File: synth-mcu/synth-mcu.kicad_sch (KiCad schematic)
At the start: 5 parts, among them J1 LoopMatrix, J2 AudioControls, J3 Conn_01x25_Socket, J4 Conn_01x25_Socket, J5 AUXOut

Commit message: add mounting holes to mcu pcb
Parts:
- added H1, H2, H3, H4: MountingHole, MountingHole:MountingHole_3.2mm_M3, symbol Mechanical:MountingHole
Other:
- note removed: "PC0 PC1 PC2 PC3 PA7 PC4 PC5 PB0 PB1"

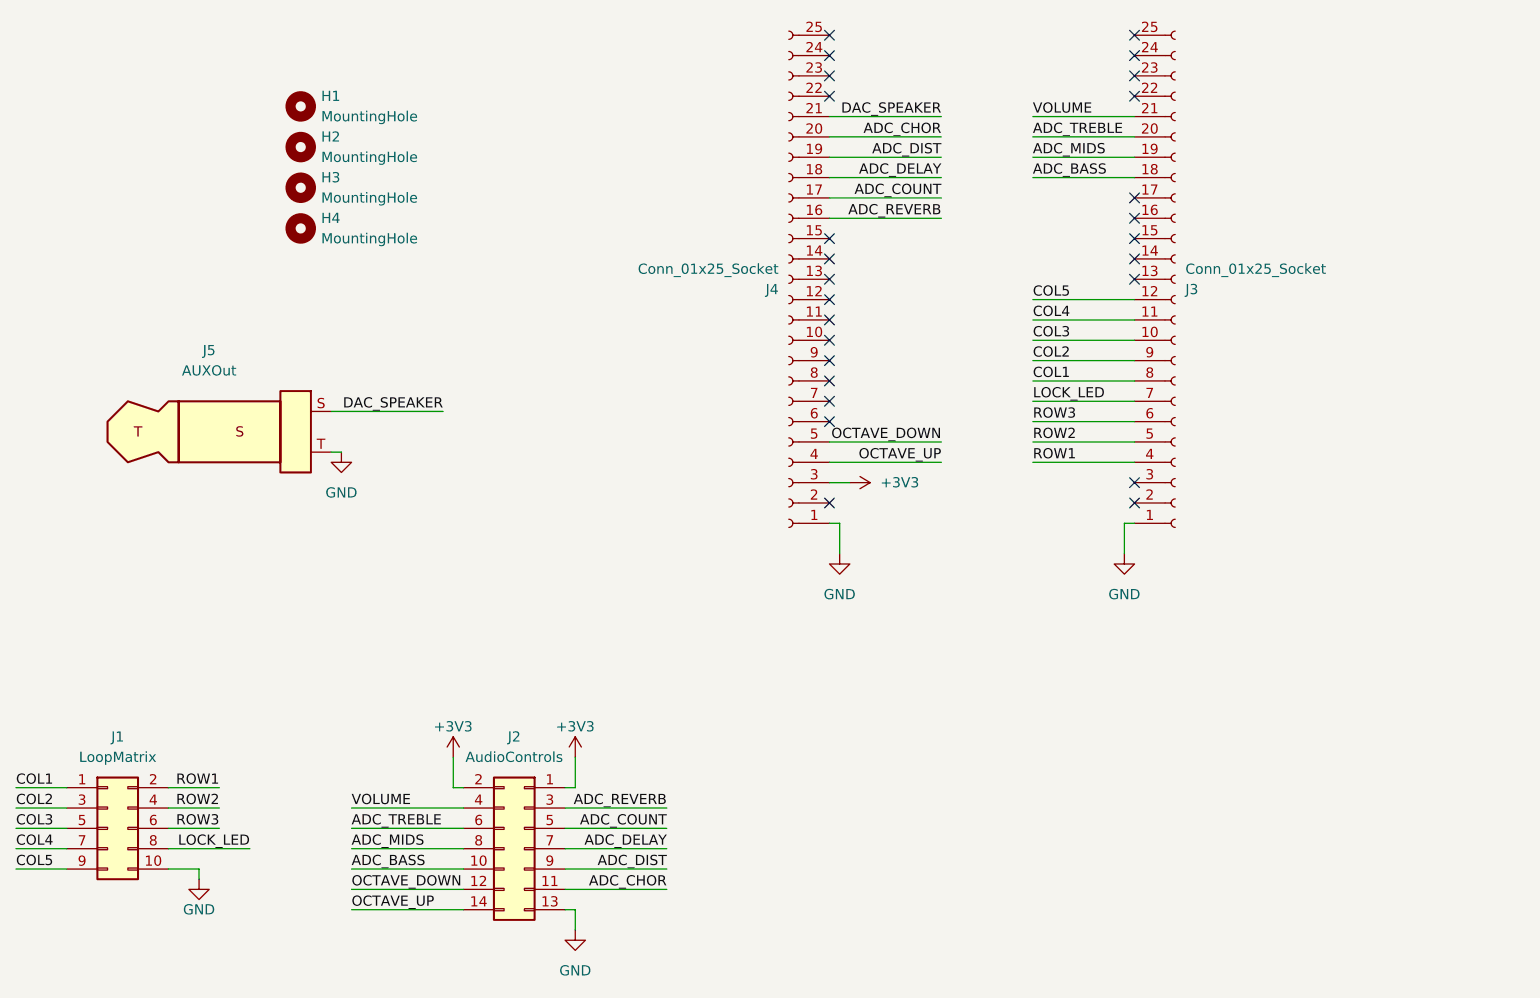
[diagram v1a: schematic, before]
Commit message: GPIO breakout for MCU board
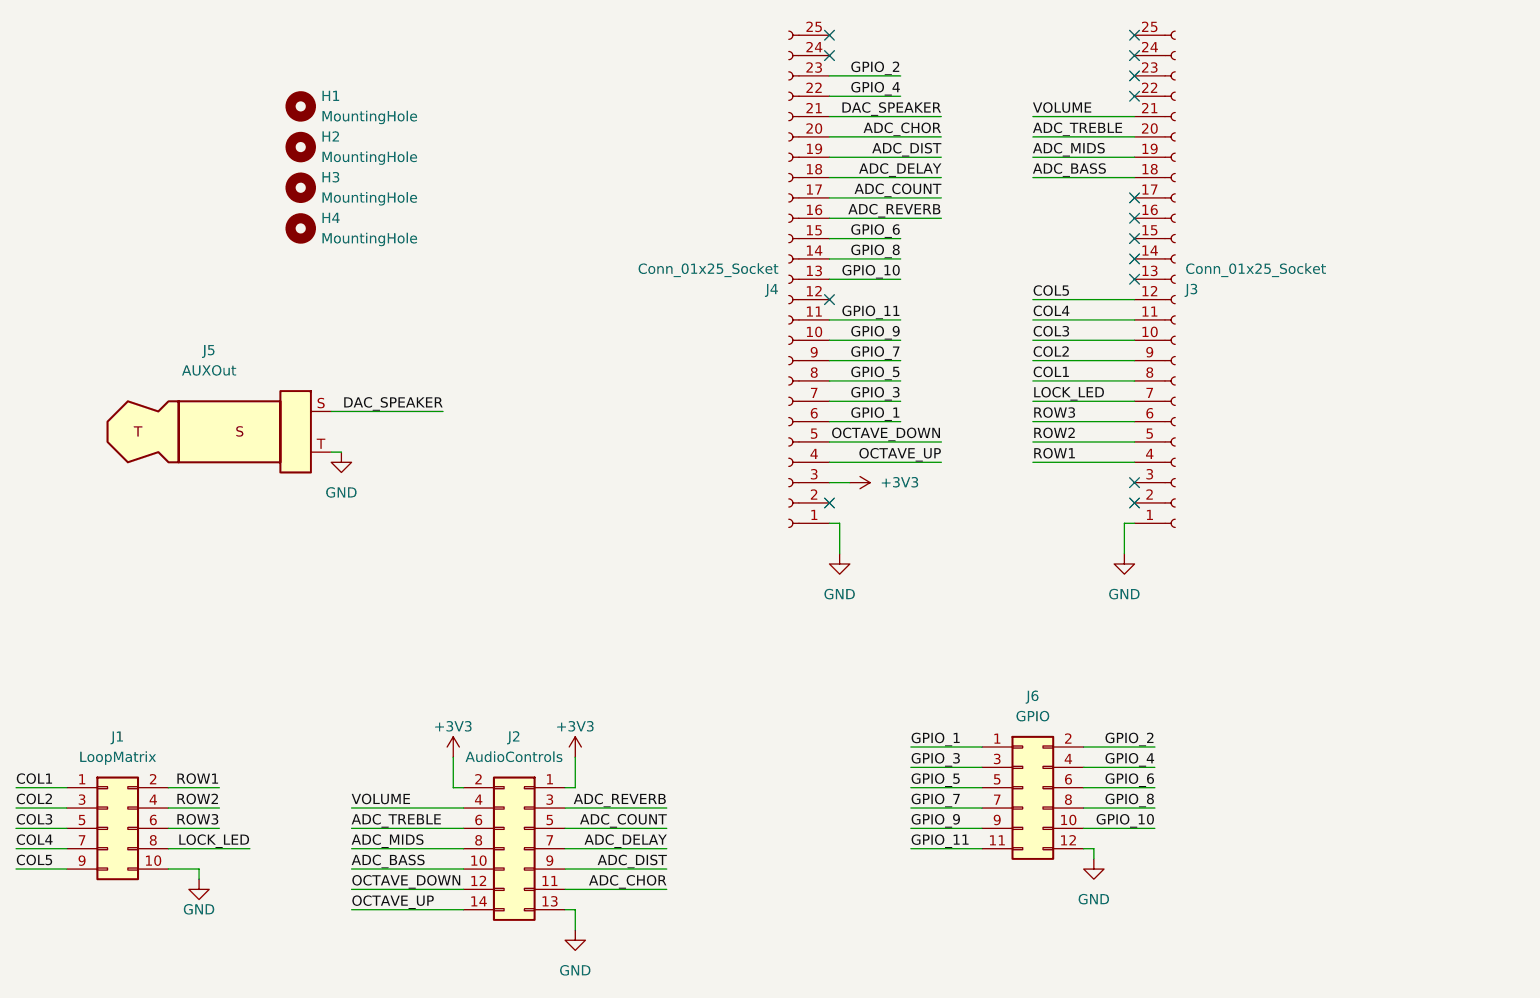
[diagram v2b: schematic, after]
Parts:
- added J6: GPIO, Connector_IDC:IDC-Header_2x06_P2.54mm_Vertical, symbol Connector_Generic:Conn_02x06_Odd_Even
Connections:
- net GND: now also J6.12 (Pin_12)
- net GPIO_9: now reaches J4.10 (Pin_10)
- net GPIO_9: now also J6.9 (Pin_9)
- net GPIO_11: now reaches J4.11 (Pin_11)
- net GPIO_11: now also J6.11 (Pin_11)
- net GPIO_10: now reaches J4.13 (Pin_13)
- net GPIO_10: now also J6.10 (Pin_10)
- net GPIO_8: now reaches J4.14 (Pin_14)
- net GPIO_8: now also J6.8 (Pin_8)
- net GPIO_6: now reaches J4.15 (Pin_15)
- net GPIO_6: now also J6.6 (Pin_6)
- net GPIO_4: now reaches J4.22 (Pin_22)
- net GPIO_4: now also J6.4 (Pin_4)
- net GPIO_2: now reaches J4.23 (Pin_23)
- net GPIO_2: now also J6.2 (Pin_2)
- net GPIO_1: now reaches J4.6 (Pin_6)
- net GPIO_1: now also J6.1 (Pin_1)
- net GPIO_3: now reaches J4.7 (Pin_7)
- net GPIO_3: now also J6.3 (Pin_3)
- net GPIO_5: now reaches J4.8 (Pin_8)
- net GPIO_5: now also J6.5 (Pin_5)
- net GPIO_7: now reaches J4.9 (Pin_9)
- net GPIO_7: now also J6.7 (Pin_7)
- no-connect marks 26 -> 15

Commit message: implement design suggestions from TA
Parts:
- removed J6: GPIO, Connector_IDC:IDC-Header_2x06_P2.54mm_Vertical, symbol Connector_Generic:Conn_02x06_Odd_Even
- added J7: GPIO, Connector_IDC:IDC-Header_2x07_P2.54mm_Vertical, symbol Connector_Generic:Conn_02x07_Odd_Even
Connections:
- net GND: now also J7.14 (Pin_14)
- net GPIO_1: now also J7.1 (Pin_1)
- net GPIO_10: now also J7.10 (Pin_10)
- net GPIO_11: now also J7.11 (Pin_11)
- net GPIO_2: now also J7.2 (Pin_2)
- net GPIO_3: now also J7.3 (Pin_3)
- net GPIO_4: now also J7.4 (Pin_4)
- net GPIO_5: now also J7.5 (Pin_5)
- net GPIO_6: now also J7.6 (Pin_6)
- net GPIO_7: now also J7.7 (Pin_7)
- net GPIO_8: now also J7.8 (Pin_8)
- net GPIO_9: now also J7.9 (Pin_9)
- new net GPIO_12: J7.12 (Pin_12)
- new net GPIO_13: J7.13 (Pin_13)
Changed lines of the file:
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@@
+	(wire
+		(pts
+			(xy 162.56 137.16) (xy 171.45 137.16)
+		)
+		(stroke
+			(width 0)
+			(type default)
+		)
+	)
 	(wire
 		(pts
@@
 	(wire
 		(pts
-			(xy 185.42 135.89) (xy 185.42 134.62)
-		)
-		(stroke
-			(width 0)
-			(type default)
-		)
-	)
-	(wire
-		(pts
 			(xy 90.17 80.01) (xy 104.14 80.01)
 		)
@@
 	(wire
 		(pts
+			(xy 185.42 137.16) (xy 184.15 137.16)
+		)
+		(stroke
+			(width 0)
+			(type default)
+		)
+	)
+	(wire
+		(pts
 			(xy 177.8 50.8) (xy 190.5 50.8)
 		)
@@
 	(wire
 		(pts
+			(xy 185.42 138.43) (xy 185.42 137.16)
+		)
+		(stroke
+			(width 0)
+			(type default)
+		)
+	)
+	(wire
+		(pts
 			(xy 120.65 123.19) (xy 120.65 127)
 		)
@@
 	(wire
 		(pts
-			(xy 184.15 134.62) (xy 185.42 134.62)
+			(xy 184.15 134.62) (xy 193.04 134.62)
 		)
 		(stroke
@@
 		)
 	)
+	(label "GPIO_12"
+		(at 193.04 134.62 180)
+		(effects
+			(font
+				(size 1.27 1.27)
+			)
+			(justify right bottom)
+		)
+	)
 	(label "LOCK_LED"
 		(at 177.8 78.74 0)
@@
 			)
 			(justify right bottom)
+		)
+	)
+	(label "GPIO_13"
+		(at 162.56 137.16 0)
+		(effects
+			(font
+				(size 1.27 1.27)
+			)
+			(justify left bottom)
 		)
 	)
@@
 	)
 	(symbol
-		(lib_id "Connector_Generic:Conn_02x06_Odd_Even")
-		(at 176.53 127 0)
-		(unit 1)
-		(body_style 1)
-		(exclude_from_sim no)
-		(in_bom yes)
-		(on_board yes)
-		(in_pos_files yes)
-		(dnp no)
-		(fields_autoplaced yes)
-		(property "Reference" "J6"
-			(at 177.8 115.57 0)
-			(show_name no)
-			(do_not_autoplace no)
-			(effects
-				(font
-					(size 1.27 1.27)
-				)
-			)
-		)
-		(property "Value" "GPIO"
-			(at 177.8 118.11 0)
-			(show_name no)
-			(do_not_autoplace no)
-			(effects
-				(font
-					(size 1.27 1.27)
-				)
-			)
-		)
-		(property "Footprint" "Connector_IDC:IDC-Header_2x06_P2.54mm_Vertical"
-			(at 176.53 127 0)
-			(hide yes)
-			(show_name no)
-			(do_not_autoplace no)
-			(effects
-				(font
-					(size 1.27 1.27)
-				)
-			)
-		)
-		(property "Datasheet" ""
-			(at 176.53 127 0)
-			(hide yes)
-			(show_name no)
-			(do_not_autoplace no)
-			(effects
-				(font
-					(size 1.27 1.27)
-				)
-			)
-		)
-		(property "Description" "Generic connector, double row, 02x06, odd/even pin numbering scheme (row 1 odd numbers, row 2 even numbers), script generated (kicad-library-utils/schlib/autogen/connector/)"
-			(at 176.53 127 0)
-			(hide yes)
-			(show_name no)
-			(do_not_autoplace no)
-			(effects
-				(font
-					(size 1.27 1.27)
-				)
-			)
-		)
-		(pin "12"
-		)
-		(pin "11"
-		)
-		(pin "1"
-		)
-		(pin "8"
-		)
-		(pin "7"
-		)
-		(pin "10"
-		)
-		(pin "9"
-		)
-		(pin "3"
-		)
-		(pin "5"
-		)
-		(pin "2"
-		)
-		(pin "4"
-		)
-		(pin "6"
-		)
-		(instances
-			(project "synth-mcu"
-				(path "/c088e41c-dfaf-4c9b-ad71-cd5bad59edb3"
-					(reference "J6")
-					(unit 1)
-				)
-			)
-		)
-	)
-	(symbol
 		(lib_id "power:GND")
 		(at 73.66 138.43 0)
@@
 	)
 	(symbol
+		(lib_id "power:GND")
+		(at 185.42 138.43 0)
+		(unit 1)
+		(body_style 1)
+		(exclude_from_sim no)
+		(in_bom yes)
+		(on_board yes)
+		(in_pos_files yes)
+		(dnp no)
+		(fields_autoplaced yes)
+		(property "Reference" "#PWR05"
+			(at 185.42 144.78 0)
+			(hide yes)
+			(show_name no)
+			(do_not_autoplace no)
+			(effects
+				(font
+					(size 1.27 1.27)
+				)
+			)
+		)
+		(property "Value" "GND"
+			(at 185.42 143.51 0)
+			(show_name no)
+			(do_not_autoplace no)
+			(effects
+				(font
+					(size 1.27 1.27)
+				)
+			)
+		)
+		(property "Footprint" ""
+			(at 185.42 138.43 0)
+			(hide yes)
+			(show_name no)
+			(do_not_autoplace no)
+			(effects
+				(font
+					(size 1.27 1.27)
+				)
+			)
+		)
+		(property "Datasheet" ""
+			(at 185.42 138.43 0)
+			(hide yes)
+			(show_name no)
+			(do_not_autoplace no)
+			(effects
+				(font
+					(size 1.27 1.27)
+				)
+			)
+		)
+		(property "Description" "Power symbol creates a global label with name \"GND\" , ground"
+			(at 185.42 138.43 0)
+			(hide yes)
+			(show_name no)
+			(do_not_autoplace no)
+			(effects
+				(font
+					(size 1.27 1.27)
+				)
+			)
+		)
+		(pin "1"
+		)
+		(instances
+			(project "synth-mcu"
+				(path "/c088e41c-dfaf-4c9b-ad71-cd5bad59edb3"
+					(reference "#PWR05")
+					(unit 1)
+				)
+			)
+		)
+	)
+	(symbol
 		(lib_id "Mechanical:MountingHole")
 		(at 86.36 57.15 0)
@@
 				(path "/c088e41c-dfaf-4c9b-ad71-cd5bad59edb3"
 					(reference "H4")
+					(unit 1)
+				)
+			)
+		)
+	)
+	(symbol
+		(lib_id "Connector_Generic:Conn_02x07_Odd_Even")
+		(at 176.53 129.54 0)
+		(unit 1)
+		(body_style 1)
+		(exclude_from_sim no)
+		(in_bom yes)
+		(on_board yes)
+		(in_pos_files yes)
+		(dnp no)
+		(property "Reference" "J7"
+			(at 177.8 115.57 0)
+			(show_name no)
+			(do_not_autoplace no)
+			(effects
+				(font
+					(size 1.27 1.27)
+				)
+			)
+		)
+		(property "Value" "GPIO"
+			(at 177.8 118.11 0)
+			(show_name no)
+			(do_not_autoplace no)
+			(effects
+				(font
+					(size 1.27 1.27)
+				)
+			)
+		)
+		(property "Footprint" "Connector_IDC:IDC-Header_2x07_P2.54mm_Vertical"
+			(at 176.53 129.54 0)
+			(hide yes)
+			(show_name no)
+			(do_not_autoplace no)
+			(effects
+				(font
+					(size 1.27 1.27)
+				)
+			)
+		)
+		(property "Datasheet" ""
+			(at 176.53 129.54 0)
+			(hide yes)
+			(show_name no)
+			(do_not_autoplace no)
+			(effects
+				(font
+					(size 1.27 1.27)
+				)
+			)
+		)
+		(property "Description" "Generic connector, double row, 02x07, odd/even pin numbering scheme (row 1 odd numbers, row 2 even numbers), script generated (kicad-library-utils/schlib/autogen/connector/)"
+			(at 176.53 129.54 0)
+			(hide yes)
+			(show_name no)
+			(do_not_autoplace no)
+			(effects
+				(font
+					(size 1.27 1.27)
+				)
+			)
+		)
+		(pin "1"
+		)
+		(pin "3"
+		)
+		(pin "4"
+		)
+		(pin "5"
+		)
+		(pin "6"
+		)
+		(pin "7"
+		)
+		(pin "8"
+		)
+		(pin "9"
+		)
+		(pin "10"
+		)
+		(pin "11"
+		)
+		(pin "14"
+		)
+		(pin "13"
+		)
+		(pin "12"
+		)
+		(pin "2"
+		)
+		(instances
+			(project "synth-mcu"
+				(path "/c088e41c-dfaf-4c9b-ad71-cd5bad59edb3"
+					(reference "J7")
 					(unit 1)
 				)
@@
 					(unit 1)
 				)
-			)
-		)
-	)
-	(symbol
-		(lib_id "power:GND")
-		(at 185.42 135.89 0)
-		(unit 1)
-		(body_style 1)
-		(exclude_from_sim no)
-		(in_bom yes)
-		(on_board yes)
-		(in_pos_files yes)
-		(dnp no)
-		(fields_autoplaced yes)
-		(property "Reference" "#PWR05"
-			(at 185.42 142.24 0)
-			(hide yes)
-			(show_name no)
-			(do_not_autoplace no)
-			(effects
-				(font
-					(size 1.27 1.27)
-				)
-			)
-		)
-		(property "Value" "GND"
-			(at 185.42 140.97 0)
-			(show_name no)
-			(do_not_autoplace no)
-			(effects
-				(font
-					(size 1.27 1.27)
-				)
-			)
-		)
-		(property "Footprint" ""
-			(at 185.42 135.89 0)
-			(hide yes)
-			(show_name no)
-			(do_not_autoplace no)
-			(effects
-				(font
-					(size 1.27 1.27)
-				)
-			)
-		)
-		(property "Datasheet" ""
-			(at 185.42 135.89 0)
-			(hide yes)
-			(show_name no)
-			(do_not_autoplace no)
-			(effects
-				(font
-					(size 1.27 1.27)
-				)
-			)
-		)
-		(property "Description" "Power symbol creates a global label with name \"GND\" , ground"
-			(at 185.42 135.89 0)
-			(hide yes)
-			(show_name no)
-			(do_not_autoplace no)
-			(effects
-				(font
-					(size 1.27 1.27)
-				)
-			)
-		)
-		(pin "1"
-		)
-		(instances
-			(project "synth-mcu"
-				(path "/c088e41c-dfaf-4c9b-ad71-cd5bad59edb3"
-					(reference "#PWR05")
-					(unit 1)
-				)

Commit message: Manufacturing changes & Gerber files
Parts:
- added J6: Conn_01x05, Connector_Molex:Molex_KK-254_AE-6410-05A_1x05_P2.54mm_Vertical, symbol Connector_Generic:Conn_01x05
- added J8: GPIO2, Connector_Molex:Molex_KK-254_AE-6410-05A_1x05_P2.54mm_Vertical, symbol Connector_Generic:Conn_01x05
- J5: footprint Connector_Audio:Jack_3.5mm_Switronic_ST-005-G_horizontal -> Library:AudioConnector_2092-STX-3000-ND
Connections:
- net DAC_SPEAKER: now also J5.T; no longer J5.S
- net GND: now also J5.S, J7.1 (Pin_1), J6.1 (Pin_1), J8.1 (Pin_1); no longer J5.T, J7.14 (Pin_14)
- net GPIO_1: now also J7.3 (Pin_3); no longer J7.1 (Pin_1)
- net GPIO_10: now also J7.12 (Pin_12); no longer J7.10 (Pin_10)
- net GPIO_11: now also J7.13 (Pin_13); no longer J7.11 (Pin_11)
- net GPIO_12: now also J4.24 (Pin_24), J7.14 (Pin_14); no longer J7.12 (Pin_12)
- net GPIO_13: now also J4.12 (Pin_12), J7.2 (Pin_2); no longer J7.13 (Pin_13)
- net GPIO_2: now also J7.4 (Pin_4); no longer J7.2 (Pin_2)
- net GPIO_3: now also J7.5 (Pin_5); no longer J7.3 (Pin_3)
- net GPIO_4: now also J7.6 (Pin_6); no longer J7.4 (Pin_4)
- net GPIO_5: now also J7.7 (Pin_7); no longer J7.5 (Pin_5)
- net GPIO_6: now also J7.8 (Pin_8); no longer J7.6 (Pin_6)
- net GPIO_7: now also J7.9 (Pin_9); no longer J7.7 (Pin_7)
- net GPIO_8: now also J7.10 (Pin_10); no longer J7.8 (Pin_8)
- net GPIO_9: now also J7.11 (Pin_11); no longer J7.9 (Pin_9)
- net GPIO2_1: now reaches J3.13 (Pin_13)
- net GPIO2_1: now also J8.2 (Pin_2)
- net GPIO2_2: now reaches J3.14 (Pin_14)
- net GPIO2_2: now also J8.3 (Pin_3)
- net GPIO2_3: now reaches J3.15 (Pin_15)
- net GPIO2_3: now also J8.4 (Pin_4)
- net GPIO2_4: now reaches J3.16 (Pin_16)
- net GPIO2_4: now also J8.5 (Pin_5)
- net LED_4: now reaches J3.17 (Pin_17)
- net LED_4: now also J6.2 (Pin_2)
- net LED_1: now reaches J3.22 (Pin_22)
- net LED_1: now also J6.5 (Pin_5)
- net LED_2: now reaches J3.23 (Pin_23)
- net LED_2: now also J6.4 (Pin_4)
- net LED_3: now reaches J3.24 (Pin_24)
- net LED_3: now also J6.3 (Pin_3)
- no-connect marks 15 -> 3
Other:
- moved on the sheet: J7
